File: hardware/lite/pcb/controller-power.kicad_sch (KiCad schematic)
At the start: 10 parts, among them U1181 74HC595D,118, U1182 74HC595D,118

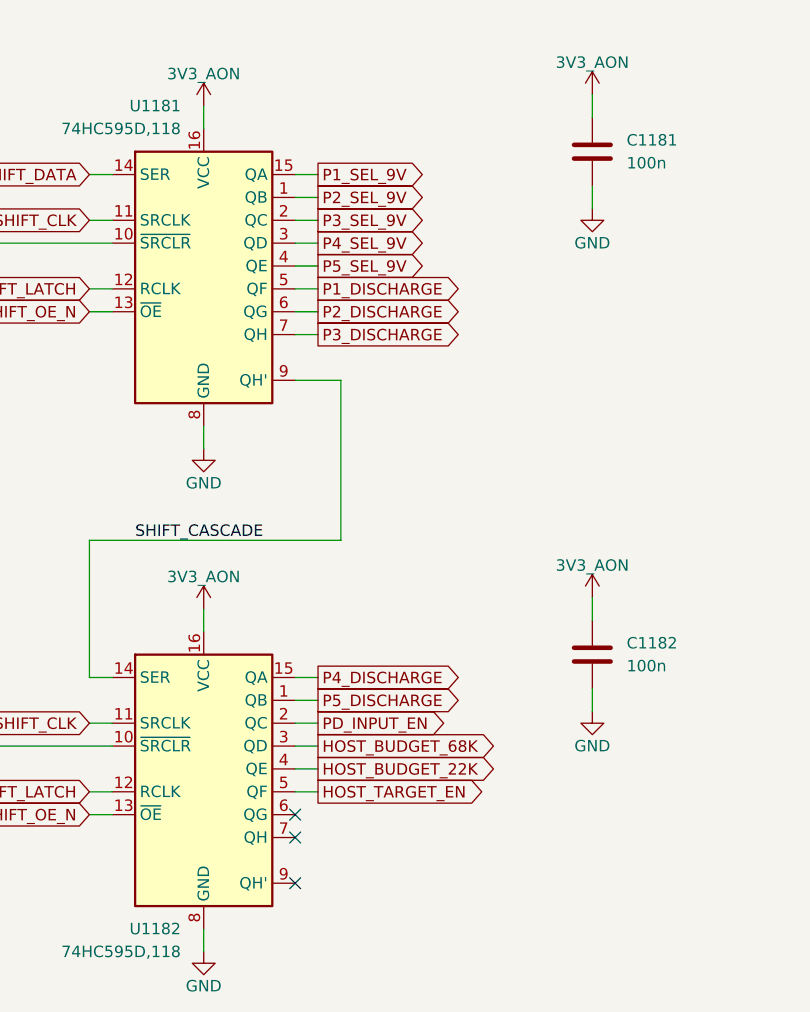
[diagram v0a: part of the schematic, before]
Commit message: feat(hardware): share brick power across ports and add CM5 link
A connected PD supply now runs the logic through its own buck and feeds
one TPS55288 buck-boost stage per port, so the contract is shared as
5-20 V at up to 5 A per port. The hub's VBUS detect becomes an OR gate,
a host-select mux lets a CM5 side board drive the hub over a 24-pin ZIF
link, and a CM5 variant joins Hub and HubPD.

The board is synced to the schematic and its old routing removed; the
new parts wait below the outline for placement.
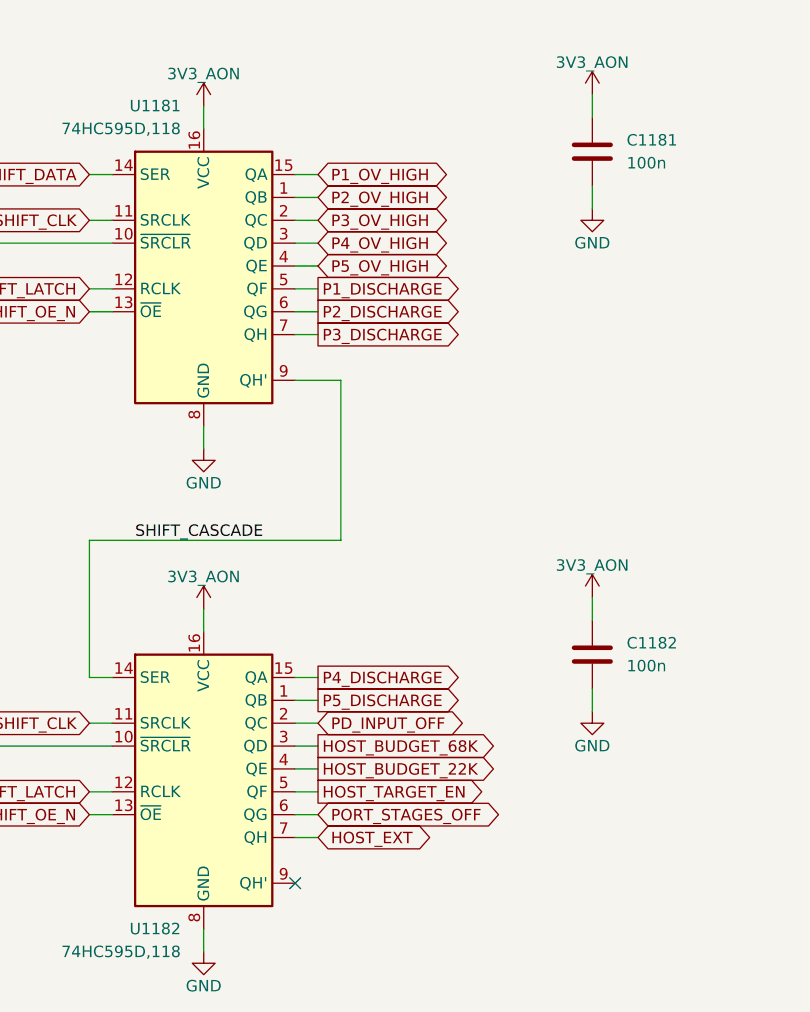
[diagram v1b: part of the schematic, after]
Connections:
- net PORT_STAGES_OFF: now reaches U1182.6 (QG)
- net HOST_EXT: now reaches U1182.7 (QH)
- net P1_SEL_9V renamed P1_OV_HIGH
- net P2_SEL_9V renamed P2_OV_HIGH
- net P3_SEL_9V renamed P3_OV_HIGH
- net P4_SEL_9V renamed P4_OV_HIGH
- net P5_SEL_9V renamed P5_OV_HIGH
- net PD_INPUT_EN renamed PD_INPUT_OFF
- no-connect marks 3 -> 1

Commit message: feat(hardware): use smaller mux, I2C switch, 595 and button packages
The TMUX1511s move to UQFN-16 (RSV), the TCA9548A to VQFN-24 (RGE),
the 74HC595s to TSSOP-16 and the BOOTSEL and RESET buttons to the
Omron B3U, which frees about 300 mm2 of the middle band. The case
button keeps the PTS645.
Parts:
- U1181, U1182: value 74HC595D,118 -> 74HC595PW; footprint Package_SO:SOIC-16_3.9x9.9mm_P1.27mm -> Package_SO:TSSOP-16_4.4x5mm_P0.65mm; LCSC C5947 -> C5948; MPN 74HC595D,118 -> 74HC595PW,118
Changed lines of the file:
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@@
 			)
 		)
-		(property "Value" "74HC595D,118"
+		(property "Value" "74HC595PW"
 			(at 93.98 48.26 0)
 			(show_name no)
@@
 			)
 		)
-		(property "Footprint" "Package_SO:SOIC-16_3.9x9.9mm_P1.27mm"
+		(property "Footprint" "Package_SO:TSSOP-16_4.4x5mm_P0.65mm"
 			(at 96.52 45.72 0)
 			(hide yes)
@@
 			)
 		)
-		(property "LCSC" "C5947"
+		(property "LCSC" "C5948"
 			(at 96.52 45.72 0)
 			(hide yes)
@@
 			)
 		)
-		(property "MPN" "74HC595D,118"
+		(property "MPN" "74HC595PW,118"
 			(at 96.52 45.72 0)
 			(hide yes)
@@
 			)
 		)
-		(property "Value" "74HC595D,118"
+		(property "Value" "74HC595PW"
 			(at 93.98 139.7 0)
 			(show_name no)
@@
 			)
 		)
-		(property "Footprint" "Package_SO:SOIC-16_3.9x9.9mm_P1.27mm"
+		(property "Footprint" "Package_SO:TSSOP-16_4.4x5mm_P0.65mm"
 			(at 96.52 101.6 0)
 			(hide yes)
@@
 			)
 		)
-		(property "LCSC" "C5947"
+		(property "LCSC" "C5948"
 			(at 96.52 101.6 0)
 			(hide yes)
@@
 			)
 		)
-		(property "MPN" "74HC595D,118"
+		(property "MPN" "74HC595PW,118"
 			(at 96.52 101.6 0)
 			(hide yes)
